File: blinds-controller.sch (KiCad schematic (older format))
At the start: 12 parts, among them J1 Jack-DC, J2 Stepper Motor, J3 DC Check, J4 JTAG, U1 MPM3610AGQV-P, U2 ESP32-S2-WROOM, U3 ULN2003A

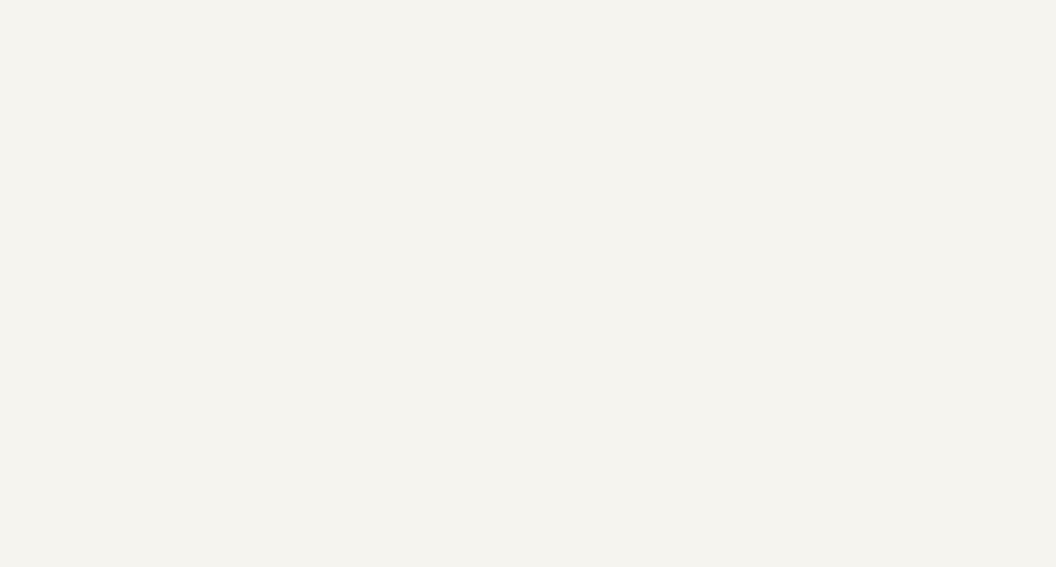
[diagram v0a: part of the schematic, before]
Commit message: Added switch symbol to library
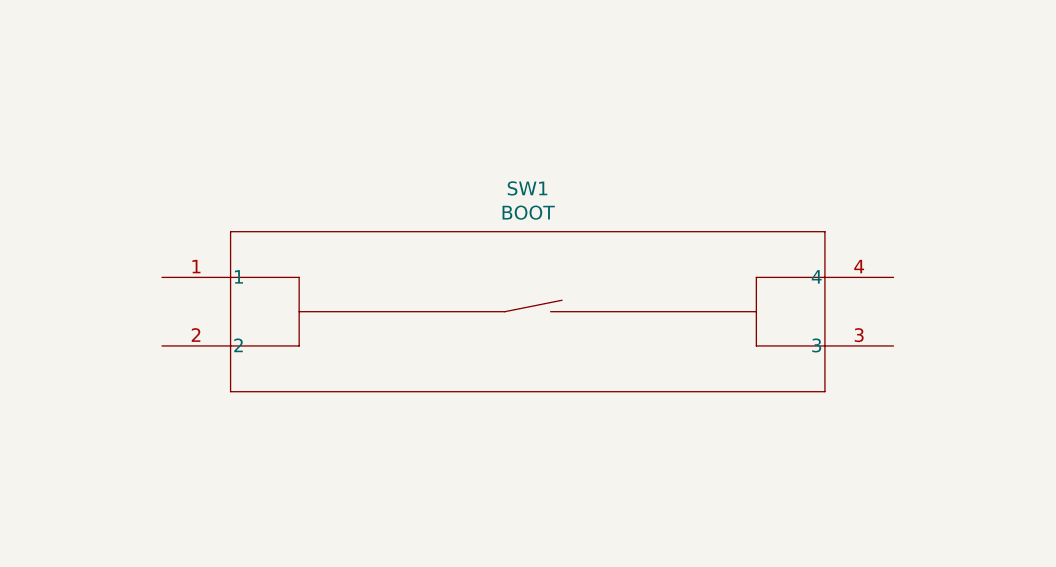
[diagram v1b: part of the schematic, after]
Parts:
- added SW1: BOOT, footprints:PTS526 SM15 SMTR2 LFS, symbol 2021-03-08_04-30-02:PTS526_SM15_SMTR2_LFS
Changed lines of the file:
@@
+	1    0    0    -1
+$EndComp
+$Comp
+L 2021-03-08_04-30-02:PTS526_SM15_SMTR2_LFS SW1
+U 1 1 6060A107
+P 3500 3000
+F 0 "SW1" H 5100 3387 60  0000 C CNN
+F 1 "BOOT" H 5100 3281 60  0000 C CNN
+F 2 "footprints:PTS526 SM15 SMTR2 LFS" H 5100 3240 60  0001 C CNN
+F 3 "" H 3500 3000 60  0000 C CNN
+	1    3500 3000
 	1    0    0    -1
 $EndComp

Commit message: Added decoupling capacitors to ESP32
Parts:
- added C3: 22uF, Capacitor_SMD:C_1206_3216Metric, symbol Device:C
- added C4: 0.1uF, Capacitor_SMD:C_1206_3216Metric, symbol Device:C
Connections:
- net +3V3: now also C3.1, C4.1
- net GND: now also C3.2, C4.2
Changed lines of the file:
@@
 L power:+3.3V #PWR0107
 U 1 1 603555C6
-P 10250 3400
-F 0 "#PWR0107" H 10250 3250 50  0001 C CNN
-F 1 "+3.3V" H 10265 3573 50  0000 C CNN
-F 2 "" H 10250 3400 50  0001 C CNN
-F 3 "" H 10250 3400 50  0001 C CNN
-	1    10250 3400
+P 10650 3400
+F 0 "#PWR0107" H 10650 3250 50  0001 C CNN
+F 1 "+3.3V" H 10665 3573 50  0000 C CNN
+F 2 "" H 10650 3400 50  0001 C CNN
+F 3 "" H 10650 3400 50  0001 C CNN
+	1    10650 3400
 	1    0    0    -1
 $EndComp
@@
 	10150 3500 10250 3500
 Wire Wire Line
-	10250 3500 10250 3400
+	10650 3500 10650 3400
 NoConn ~ 1850 7100
 NoConn ~ 3700 7100
@@
 	1    0    0    -1
 $EndComp
+$Comp
+L Device:C C4
+U 1 1 604FF326
+P 10650 3650
+F 0 "C4" H 10765 3696 50  0000 L CNN
+F 1 "0.1uF" H 10765 3605 50  0000 L CNN
+F 2 "Capacitor_SMD:C_1206_3216Metric" H 10688 3500 50  0001 C CNN
+F 3 "~" H 10650 3650 50  0001 C CNN
+	1    10650 3650
+	1    0    0    -1
+$EndComp
+$Comp
+L Device:C C3
+U 1 1 60500958
+P 10250 3650
+F 0 "C3" H 10365 3696 50  0000 L CNN
+F 1 "22uF" H 10365 3605 50  0000 L CNN
+F 2 "Capacitor_SMD:C_1206_3216Metric" H 10288 3500 50  0001 C CNN
+F 3 "~" H 10250 3650 50  0001 C CNN
+	1    10250 3650
+	1    0    0    -1
+$EndComp
+$Comp
+L power:GND #PWR?
+U 1 1 605052A7
+P 10650 3800
+F 0 "#PWR?" H 10650 3550 50  0001 C CNN
+F 1 "GND" H 10655 3627 50  0000 C CNN
+F 2 "" H 10650 3800 50  0001 C CNN
+F 3 "" H 10650 3800 50  0001 C CNN
+	1    10650 3800
+	1    0    0    -1
+$EndComp
+$Comp
+L power:GND #PWR?
+U 1 1 605066F6
+P 10250 3800
+F 0 "#PWR?" H 10250 3550 50  0001 C CNN
+F 1 "GND" H 10255 3627 50  0000 C CNN
+F 2 "" H 10250 3800 50  0001 C CNN
+F 3 "" H 10250 3800 50  0001 C CNN
+	1    10250 3800
+	1    0    0    -1
+$EndComp
+Wire Wire Line
+	10250 3500 10650 3500
+Connection ~ 10250 3500
+Connection ~ 10650 3500
 $EndSCHEMATC

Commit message: Added decoupling capacitors to ULN2003A
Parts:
- added C5: 10uF, Capacitor_SMD:C_1206_3216Metric, symbol Device:C
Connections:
- net +12V: now also C5.1
- net GND: now also C5.2
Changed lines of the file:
@@
 $EndComp
 $Comp
-L power:GND #PWR?
+L power:GND #PWR0124
 U 1 1 605052A7
 P 10650 3800
-F 0 "#PWR?" H 10650 3550 50  0001 C CNN
+F 0 "#PWR0124" H 10650 3550 50  0001 C CNN
 F 1 "GND" H 10655 3627 50  0000 C CNN
 F 2 "" H 10650 3800 50  0001 C CNN
@@
 $EndComp
 $Comp
-L power:GND #PWR?
+L power:GND #PWR0125
 U 1 1 605066F6
 P 10250 3800
-F 0 "#PWR?" H 10250 3550 50  0001 C CNN
+F 0 "#PWR0125" H 10250 3550 50  0001 C CNN
 F 1 "GND" H 10255 3627 50  0000 C CNN
 F 2 "" H 10250 3800 50  0001 C CNN
@@
 Connection ~ 10250 3500
 Connection ~ 10650 3500
+$Comp
+L Device:C C5
+U 1 1 605107BB
+P 8000 1400
+F 0 "C5" H 8115 1446 50  0000 L CNN
+F 1 "10uF" H 8115 1355 50  0000 L CNN
+F 2 "Capacitor_SMD:C_1206_3216Metric" H 8038 1250 50  0001 C CNN
+F 3 "~" H 8000 1400 50  0001 C CNN
+	1    8000 1400
+	1    0    0    -1
+$EndComp
+$Comp
+L power:+12V #PWR?
+U 1 1 60520C91
+P 8000 1250
+F 0 "#PWR?" H 8000 1100 50  0001 C CNN
+F 1 "+12V" H 8015 1423 50  0000 C CNN
+F 2 "" H 8000 1250 50  0001 C CNN
+F 3 "" H 8000 1250 50  0001 C CNN
+	1    8000 1250
+	1    0    0    -1
+$EndComp
+$Comp
+L power:GND #PWR?
+U 1 1 60521866
+P 8000 1550
+F 0 "#PWR?" H 8000 1300 50  0001 C CNN
+F 1 "GND" H 8005 1377 50  0000 C CNN
+F 2 "" H 8000 1550 50  0001 C CNN
+F 3 "" H 8000 1550 50  0001 C CNN
+	1    8000 1550
+	1    0    0    -1
+$EndComp
 $EndSCHEMATC

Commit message: Added RESET switch and made some adjustments
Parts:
- added C6: 1uf, Capacitor_SMD:C_1206_3216Metric, symbol Device:C
- added R4: 10k, Resistor_SMD:R_1206_3216Metric, symbol Device:R
- SW1: value BOOT -> RESET
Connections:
- net +3V3: now also R4.1; no longer U2.41 (EN)
- net GND: now also SW1.3, SW1.4, C6.2
- net RESET: now reaches SW1.1
- net RESET: now also SW1.2, U2.41 (EN), C6.1, R4.2
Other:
- moved on the sheet: SW1
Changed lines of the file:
@@
 Text GLabel 6100 1550 2    50   BiDi ~ 0
 JTAG.nRESET
-Wire Wire Line
-	8800 3700 8950 3700
-Wire Wire Line
-	8800 3600 8800 3700
-$Comp
-L power:+3.3V #PWR0108
-U 1 1 60356942
-P 8800 3600
-F 0 "#PWR0108" H 8800 3450 50  0001 C CNN
-F 1 "+3.3V" H 8815 3773 50  0000 C CNN
-F 2 "" H 8800 3600 50  0001 C CNN
-F 3 "" H 8800 3600 50  0001 C CNN
-	1    8800 3600
-	1    0    0    -1
-$EndComp
 $Comp
 L 2021-03-08_04-30-02:PTS526_SM15_SMTR2_LFS SW1
 U 1 1 6060A107
-P 3500 3000
-F 0 "SW1" H 5100 3387 60  0000 C CNN
-F 1 "BOOT" H 5100 3281 60  0000 C CNN
-F 2 "footprints:PTS526 SM15 SMTR2 LFS" H 5100 3240 60  0001 C CNN
-F 3 "" H 3500 3000 60  0000 C CNN
-	1    3500 3000
+P 3600 3000
+F 0 "SW1" H 5200 3387 60  0000 C CNN
+F 1 "RESET" H 5200 3281 60  0000 C CNN
+F 2 "footprints:PTS526 SM15 SMTR2 LFS" H 5200 3240 60  0001 C CNN
+F 3 "" H 3600 3000 60  0000 C CNN
+	1    3600 3000
 	1    0    0    -1
 $EndComp
@@
 $EndComp
 $Comp
-L power:+12V #PWR?
+L power:+12V #PWR0126
 U 1 1 60520C91
 P 8000 1250
-F 0 "#PWR?" H 8000 1100 50  0001 C CNN
+F 0 "#PWR0126" H 8000 1100 50  0001 C CNN
 F 1 "+12V" H 8015 1423 50  0000 C CNN
 F 2 "" H 8000 1250 50  0001 C CNN
@@
 $EndComp
 $Comp
-L power:GND #PWR?
+L power:GND #PWR0127
 U 1 1 60521866
 P 8000 1550
-F 0 "#PWR?" H 8000 1300 50  0001 C CNN
+F 0 "#PWR0127" H 8000 1300 50  0001 C CNN
 F 1 "GND" H 8005 1377 50  0000 C CNN
 F 2 "" H 8000 1550 50  0001 C CNN
@@
 	1    0    0    -1
 $EndComp
+Text GLabel 8950 3700 0    50   Input ~ 0
+RESET
+Text GLabel 3300 3150 0    50   Output ~ 0
+RESET
+Wire Wire Line
+	3300 3150 3500 3150
+Wire Wire Line
+	3500 3150 3500 3000
+Wire Wire Line
+	3500 3300 3500 3150
+Connection ~ 3500 3150
+$Comp
+L power:GND #PWR?
+U 1 1 60530FF3
+P 7000 3400
+F 0 "#PWR?" H 7000 3150 50  0001 C CNN
+F 1 "GND" H 7005 3227 50  0000 C CNN
+F 2 "" H 7000 3400 50  0001 C CNN
+F 3 "" H 7000 3400 50  0001 C CNN
+	1    7000 3400
+	1    0    0    -1
+$EndComp
+Wire Wire Line
+	6800 3000 7000 3000
+Wire Wire Line
+	7000 3000 7000 3300
+Wire Wire Line
+	6800 3300 7000 3300
+Connection ~ 7000 3300
+Wire Wire Line
+	7000 3300 7000 3400
+$Comp
+L power:+3V3 #PWR?
+U 1 1 60537FE1
+P 3500 2700
+F 0 "#PWR?" H 3500 2550 50  0001 C CNN
+F 1 "+3V3" H 3515 2873 50  0000 C CNN
+F 2 "" H 3500 2700 50  0001 C CNN
+F 3 "" H 3500 2700 50  0001 C CNN
+	1    3500 2700
+	1    0    0    -1
+$EndComp
+$Comp
+L Device:R R4
+U 1 1 60537FE7
+P 3500 2850
+F 0 "R4" H 3570 2896 50  0000 L CNN
+F 1 "10k" H 3570 2805 50  0000 L CNN
+F 2 "Resistor_SMD:R_1206_3216Metric" V 3430 2850 50  0001 C CNN
+F 3 "~" H 3500 2850 50  0001 C CNN
+	1    3500 2850
+	1    0    0    -1
+$EndComp
+Wire Wire Line
+	3600 3000 3500 3000
+Connection ~ 3500 3000
+Wire Wire Line
+	3600 3300 3500 3300
+$Comp
+L Device:C C6
+U 1 1 605445FE
+P 3500 3450
+F 0 "C6" H 3615 3496 50  0000 L CNN
+F 1 "1uf" H 3615 3405 50  0000 L CNN
+F 2 "Capacitor_SMD:C_1206_3216Metric" H 3538 3300 50  0001 C CNN
+F 3 "~" H 3500 3450 50  0001 C CNN
+	1    3500 3450
+	1    0    0    -1
+$EndComp
+Connection ~ 3500 3300
+$Comp
+L power:GND #PWR?
+U 1 1 6054C09C
+P 3500 3600
+F 0 "#PWR?" H 3500 3350 50  0001 C CNN
+F 1 "GND" H 3505 3427 50  0000 C CNN
+F 2 "" H 3500 3600 50  0001 C CNN
+F 3 "" H 3500 3600 50  0001 C CNN
+	1    3500 3600
+	1    0    0    -1
+$EndComp
